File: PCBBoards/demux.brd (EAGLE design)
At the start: 108.4 x 161.5 mm, 106 parts, among them IC1 4013N, IC2 4013N, IC3 4013N, IC4 4013N, IC5 4013N, IC6 4013N, IC7 4069N, IC8 4069N, Q1 2N3904, Q10 2N3904, Q11 2N3904, Q12 2N3904, Q2 2N3904, Q3 2N3904, Q4 2N3904, Q5 2N3904, Q6 2N3904, Q7 2N3904, Q8 2N3904, Q9 2N3904, T1 2N3904, T2 2N3904, T3 2N3904, T4 2N3904, T5 2N3904, T6 2N3904

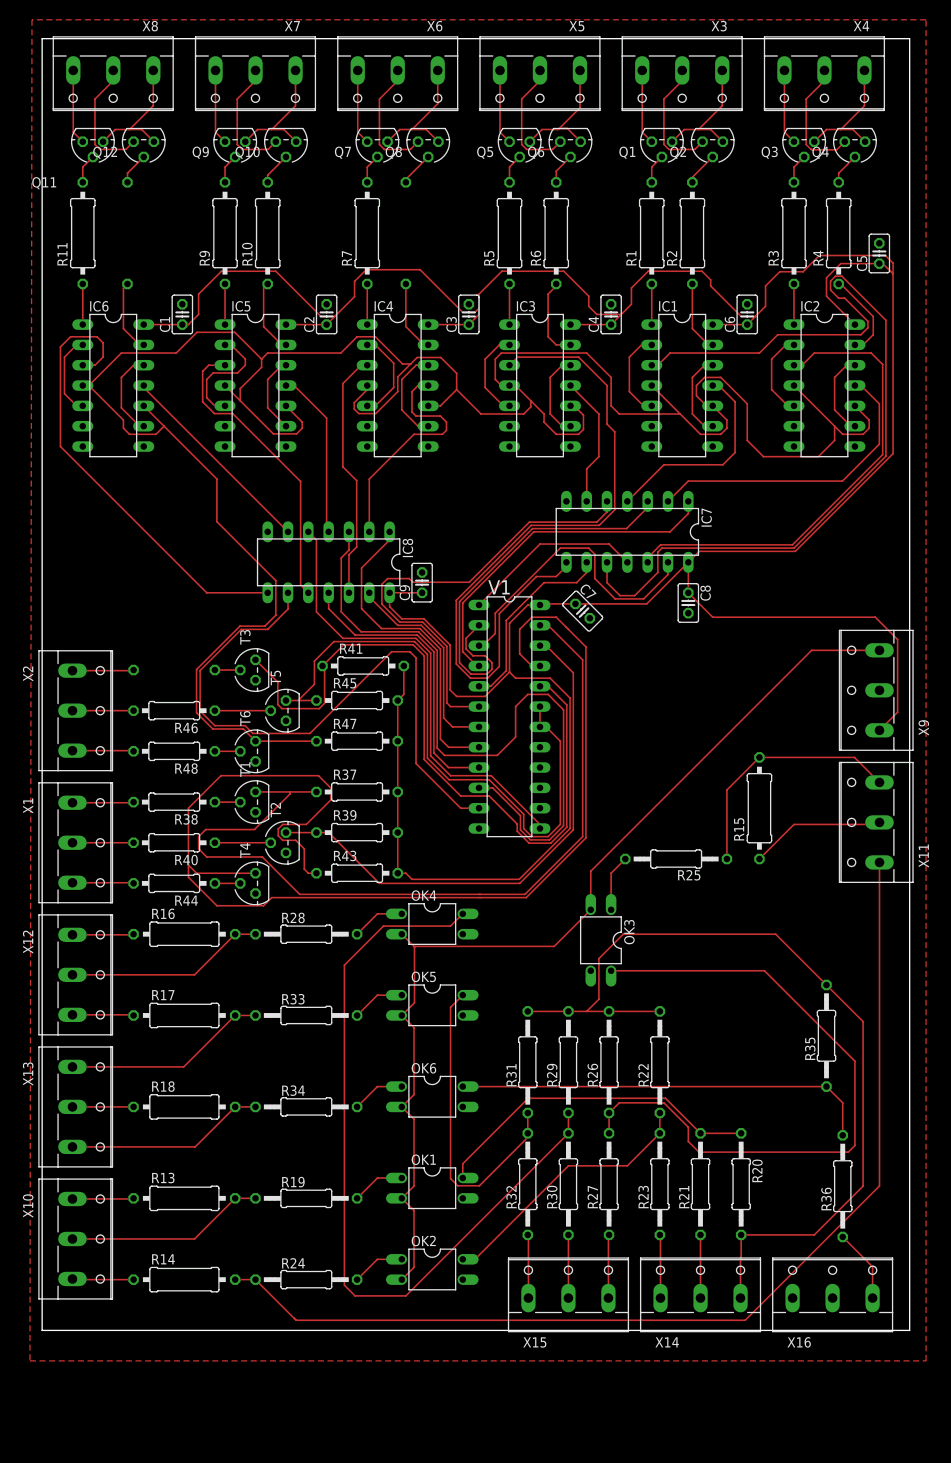
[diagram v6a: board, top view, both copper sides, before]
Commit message: FR/SR updated to 74HC**
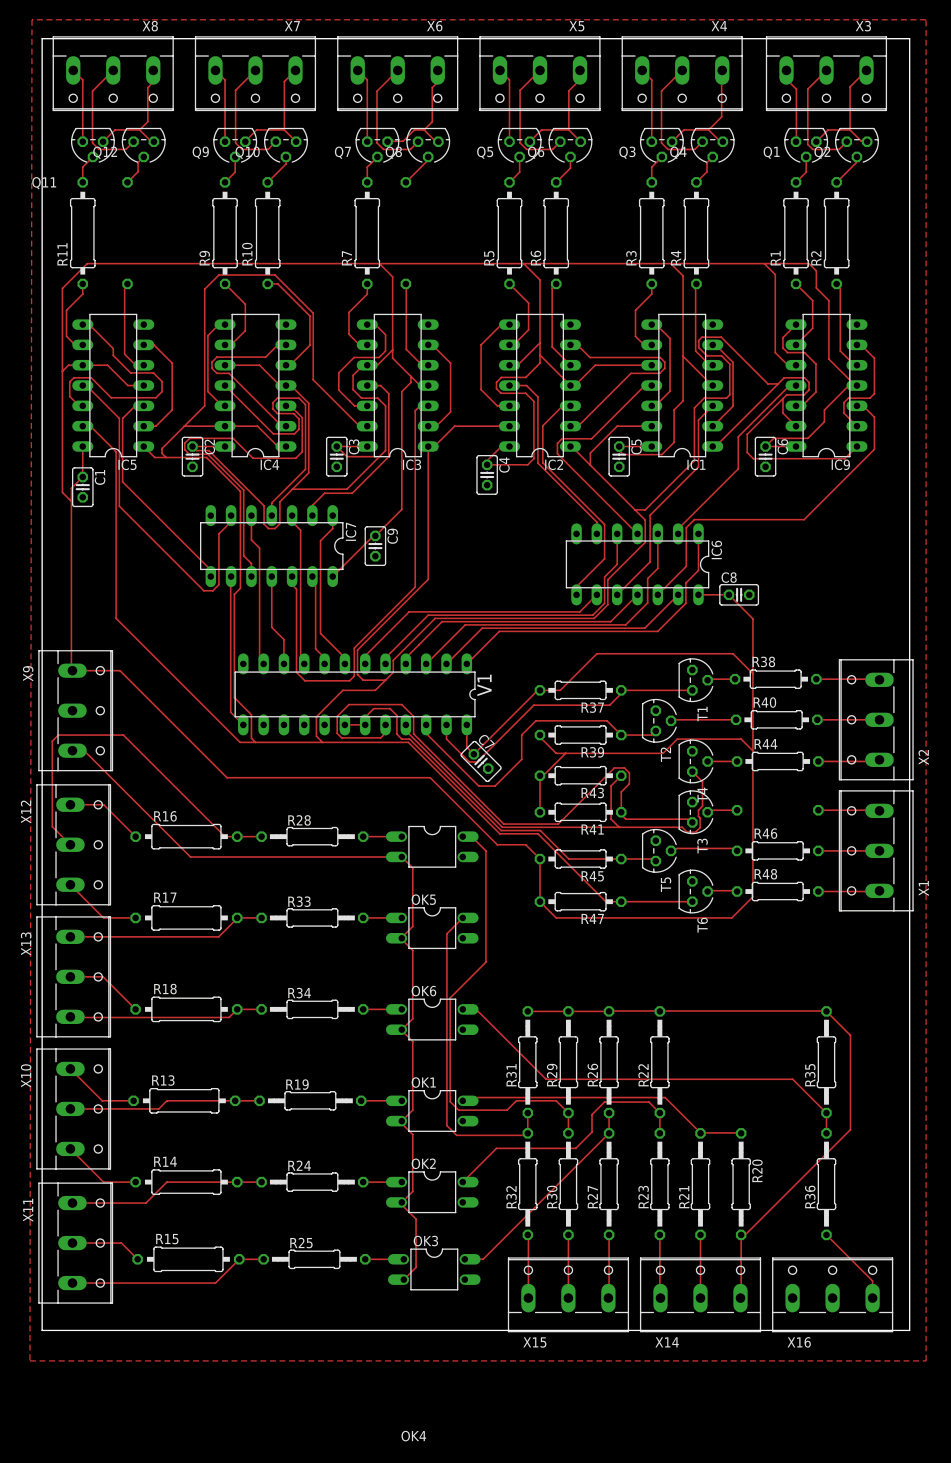
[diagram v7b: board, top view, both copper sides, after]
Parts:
- removed IC8: 4069N, 40xx:DIL14
- added IC9: 74HC74N, 74xx-eu:DIL14
- IC1, IC2, IC3, IC4, IC5: value 4013N -> 74HC74N; device 40xx:DIL14 -> 74xx-eu:DIL14
- IC6: value 4013N -> 74HC04N; device 40xx:DIL14 -> 74xx-eu:DIL14
- IC7: value 4069N -> 74HC04N; device 40xx:DIL14 -> 74xx-eu:DIL14
- moved X11 111.5 mm to (5.08, -57.7), turned to 270 degrees
- moved X9 98.3 mm to (5.08, 8.89), turned to 270 degrees
- moved X2 98.3 mm to (103.4, 7.75), turned to 90 degrees
- moved X1 98.3 mm to (103.4, -8.64), turned to 90 degrees
- moved R15 91.0 mm to (18.3, -59.7), turned to 0 degrees
- moved R42 77.4 mm to (91.9, -3.56), turned to 180 degrees
- moved R46 77.4 mm to (91.9, -8.64), turned to 0 degrees
- moved R48 77.4 mm to (91.9, -13.7), turned to 0 degrees
- moved R44 77.0 mm to (91.9, 2.54), turned to 0 degrees
- moved R40 76.9 mm to (91.8, 7.75), turned to 0 degrees
- moved R38 76.7 mm to (91.7, 12.8), turned to 0 degrees
- moved IC6 69.2 mm to (74.4, 27.2), turned to 180 degrees
- moved R25 67.4 mm to (34.0, -59.7), turned to 0 degrees
- moved T3 57.4 mm to (81.3, -3.81), turned to 270 degrees
- moved T6 57.4 mm to (81.3, -13.7), turned to 270 degrees
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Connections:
- removed net N$36: IC6.12, IC6.9
- new net N$24: IC1.3, IC6.10
- net +5V: now also IC1.10, IC1.4, IC2.10, IC2.4, IC3.10, IC3.4, IC4.10, IC4.4, IC5.10, IC5.4, IC9.10, IC9.14, IC9.4; no longer IC8.14
- net GND: now also IC9.7; no longer IC1.6, IC1.8, IC2.6, IC2.8, IC3.6, IC3.8, IC4.6, IC4.8, IC5.6, IC5.8, IC6.6, IC6.8, IC8.7
- net GPIO1: now also X2.3; no longer X1.1
- net GPIO2: now also X2.2; no longer X1.2
- net GPIO3: now also X2.1; no longer X1.3
- net GPIO4: now also X1.3; no longer X2.1
- net GPIO5: now also X1.2; no longer X2.2
- net GPIO6: now also X1.1; no longer X2.3
- net IN_5: now also IC1.1, IC1.13, IC2.1, IC2.13, IC3.1, IC3.13, IC4.1, IC4.13, IC5.1, IC5.13, IC9.1, IC9.13; no longer IC1.10, IC1.4, IC2.10, IC2.4, IC3.10, IC3.4, IC4.10, IC4.4, IC5.10, IC5.4, IC6.10, IC6.4
- net N$1: now also IC4.11, IC7.4; no longer IC2.3, IC7.12
- net N$10: now also IC7.11; no longer IC8.3
- net N$11: now also IC4.3, IC7.10; no longer IC6.3, IC8.8
- net N$12: now also IC6.12, IC9.3; no longer IC1.2, IC1.5
- net N$13: now also IC5.3, IC7.8; no longer IC3.11, IC7.6
- net N$14: now also IC9.2, IC9.6; no longer IC1.12, IC1.9
- net N$15: now also IC1.11, IC6.4; no longer IC2.2, IC2.5
- net N$16: now also IC5.11, IC7.6; no longer IC2.12, IC2.9
- net N$17: now also IC3.11, IC7.2; no longer IC3.2, IC3.5
- net N$18: now also IC2.2, IC2.6; no longer IC3.12, IC3.9
- net N$19: now also IC3.3, IC7.12; no longer IC4.2, IC4.5
- net N$2: now also IC1.2, IC1.6; no longer IC2.11, IC7.2
- net N$20: now also IC4.2, IC4.6; no longer IC4.12, IC4.9
- net N$21: now also IC1.12, IC1.8; no longer IC5.2, IC5.5
- net N$22: now also IC2.3, IC6.8; no longer IC5.12, IC5.9
- net N$23: now also IC2.11, IC6.6; no longer IC6.2, IC6.5
- net N$25: now also IC6.13; no longer IC7.3
- net N$26: now also IC6.3; no longer IC7.13
- net N$27: now also IC6.11; no longer IC7.1
- net N$28: now also IC6.5; no longer IC7.9
- net N$29: now also IC6.9; no longer IC7.5
- net N$3: now also IC9.12, IC9.8; no longer IC1.11, IC7.4
- net N$30: now also IC7.1; no longer IC8.13
- net N$31: now also IC7.13; no longer IC8.1
- net N$32: now also IC4.12, IC4.8; no longer IC5.11, IC8.4
- net N$33: now also IC5.12, IC5.8; no longer IC5.3, IC8.10
- net N$34: now also IC7.5; no longer IC8.9
- net N$35: now also IC7.9; no longer IC8.5
- net N$37: now also IC9.9; no longer IC1.1
- net N$4: now also IC6.2, IC9.11; no longer IC1.3, IC7.10
- net N$40: now also IC9.5; no longer IC1.13
- net N$41: now also IC1.9; no longer IC2.1
- net N$44: now also IC1.5; no longer IC2.13
- net N$45: now also IC2.9; no longer IC3.1
- net N$48: now also IC2.5; no longer IC3.13
- net N$49: now also IC3.9; no longer IC4.1
- net N$5: now also IC6.1; no longer IC7.11
- net N$52: now also IC3.5; no longer IC4.13
- net N$53: now also IC4.9; no longer IC5.1
- net N$56: now also IC4.5; no longer IC5.13
- net N$57: now also IC5.9; no longer IC6.1
- net N$6: now also IC3.12, IC3.8; no longer IC4.3, IC8.12
- net N$60: now also IC5.5; no longer IC6.13
- net N$7: now also IC3.2, IC3.6; no longer IC4.11, IC8.2
- net N$8: now also IC2.12, IC2.8; no longer IC3.3, IC7.8
- net N$82: now also IC7.3; no longer IC8.11
- net N$9: now also IC5.2, IC5.6; no longer IC6.11, IC8.6
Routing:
- net +5V: track 404.3 -> 688.0 mm
- net IN_5: track 302.4 -> 452.8 mm
- net FREQ2: track 130.0 -> 24.7 mm
- net IN_2: track 151.4 -> 58.5 mm
- net N$4: track 110.4 -> 25.1 mm
- net N$10: track 88.5 -> 11.6 mm
- net N$8: track 87.1 -> 14.6 mm
- net IN_0: track 105.6 -> 37.7 mm
- net N$34: track 77.3 -> 19.2 mm
- net N$67: track 83.4 -> 27.1 mm
- net N$19: track 11.5 -> 58.3 mm
- net N$66: track 97.0 -> 55.7 mm
- net N$35: track 57.4 -> 19.2 mm
- net N$16: track 10.6 -> 43.7 mm
- net N$12: track 11.3 -> 44.2 mm
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
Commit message: update SR/FR board
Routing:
- net +5V: track 688.0 -> 685.6 mm
